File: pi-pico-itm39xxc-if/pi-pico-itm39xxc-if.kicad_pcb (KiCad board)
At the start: 2 copper layers, 113 parts, among them J10 Conn_01x03, J11 Conn_02x04_Odd_Even, J3 Conn_01x03, J4 Conn_01x02, J5 Conn_02x05_Odd_Even, J6 Conn_01x10, J8 Conn_01x02, J9 Conn_01x02, U1 Pico, U10 Opamp_Dual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

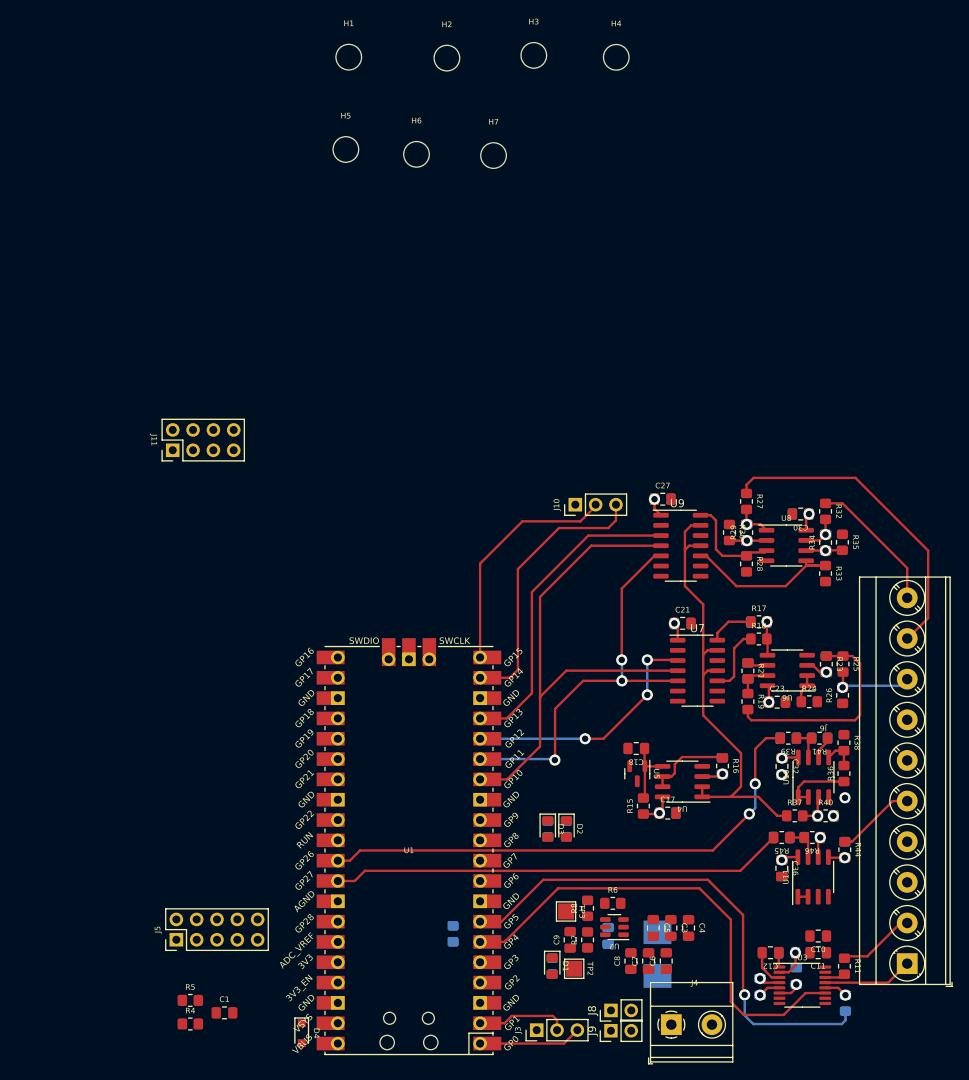
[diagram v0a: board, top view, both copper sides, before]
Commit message: Finishing pi pico itm if pcb
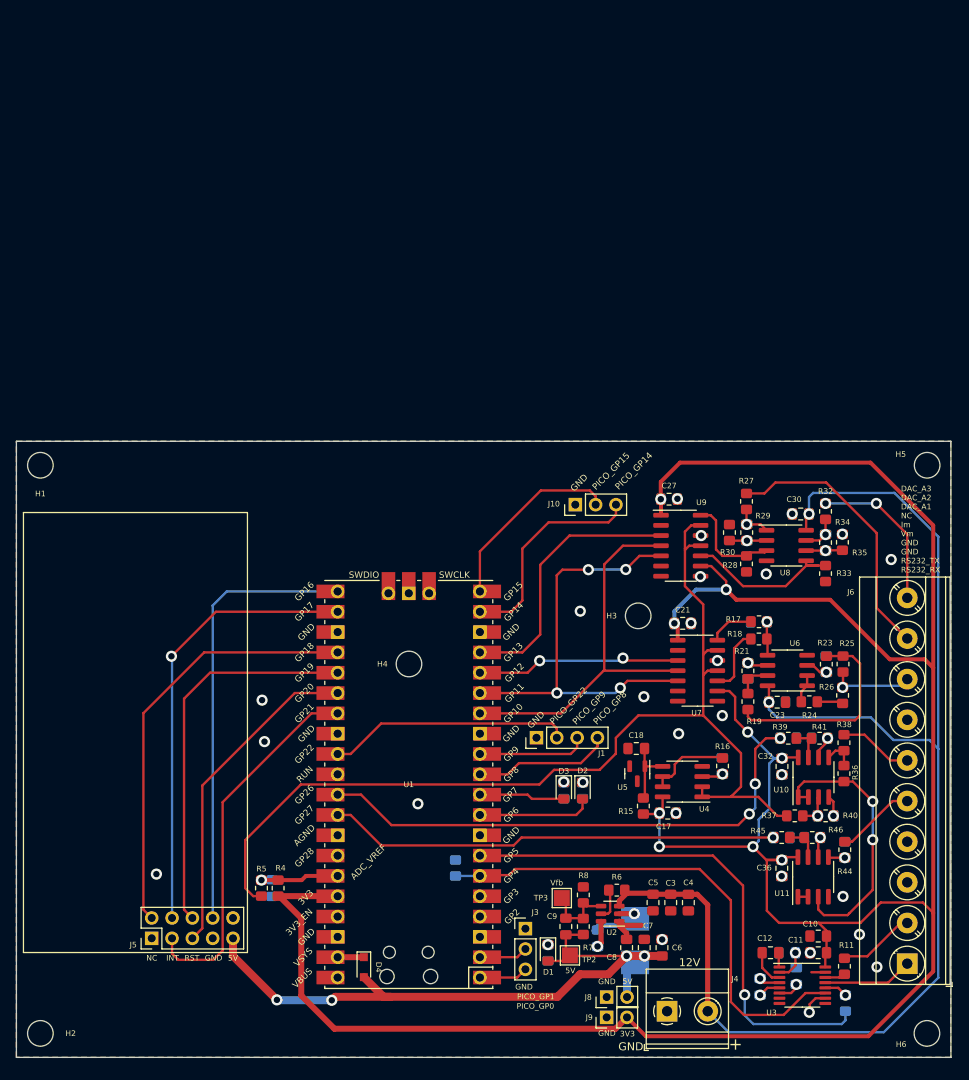
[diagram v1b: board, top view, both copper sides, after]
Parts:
- removed H7: MountingHole, MountingHole:MountingHole_3.2mm_M3
- removed J11: Conn_02x04_Odd_Even, Connector_PinHeader_2.54mm:PinHeader_2x04_P2.54mm_Vertical
- added J1: Conn_01x04, Connector_PinHeader_2.54mm:PinHeader_1x04_P2.54mm_Vertical, F.Cu at (122.2, 69.4)
- C1: moved to B.Cu
- moved H2 132.1 mm to (60.2, 106.4)
- moved H6 127.1 mm to (171.0, 106.4)
- moved H5 82.7 mm to (171.0, 35.4)
- moved H4 80.1 mm to (106.2, 60.2)
- moved H3 71.3 mm to (134.9, 54.2)
- moved H1 63.9 mm to (60.2, 35.4)
- moved R4 20.2 mm to (89.9, 88.2), turned to 90 degrees
- moved C1 16.7 mm to (89.1, 88.2), turned to -90 degrees
- moved R5 16.6 mm to (87.8, 88.2), turned to 90 degrees
- moved J3 12.8 mm to (120.8, 93.3), turned to 0 degrees
- moved D4 11.3 mm to (100.6, 98.1)
- moved U1 8.26 mm to (106.2, 75.3)
- moved R10 8.24 mm to (112.1, 85.7)
- moved D2 5.19 mm to (127.9, 76.1)
- moved R2 5.19 mm to (127.9, 76.1)
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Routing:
- net +3V3: track 13.1 -> 343.6 mm, vias 5 -> 9
- net +12V: track 4.31 -> 163.1 mm
- net +5V: track 0.00 -> 84.6 mm, vias 0 -> 4
- net /DAC_REF: track 57.8 -> 131.1 mm
- net /PICO_GPIO17: track 0.00 -> 55.8 mm, vias 0 -> 1
- net /PICO_GPIO16: track 0.00 -> 55.4 mm
- net /PICO_GPIO18: track 0.00 -> 53.5 mm
- net /PICO_GPIO19: track 0.00 -> 48.4 mm
- net /PICO_GPIO21: track 0.00 -> 46.6 mm
- net /PICO_GPIO20: track 0.00 -> 41.3 mm
- net /PICO_GPIO22: track 0.00 -> 30.4 mm
- net /itm39xxc_meas_cond/V_ref': track 8.49 -> 34.2 mm, vias 0 -> 2
- net /PICO_GPIO8: track 0.00 -> 17.2 mm
- net /DAC_SCLK: track 64.4 -> 48.3 mm
- net /LED_1: track 0.00 -> 14.4 mm
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- added copper zone on B.Cu, net GND
- added copper zone on F.Cu, net GND
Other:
- board outline added: 116.8 x 77 mm
- board text added: "+"
- board text added: "12V"
- board text added: "3V3"
- board text added: "5V"
- board text added: "DAC_A3 DAC_A2 DAC_A1 NC Im Vm GND GND RS232_TX RS232_RX"
- board text added: "GND"
- board text added: "INT"
- board text added: "NC"
- board text added: "PICO_GP0"
- board text added: "PICO_GP1"
- board text added: "PICO_GP14"
- board text added: "PICO_GP15"
- board text added: "PICO_GP22"
- board text added: "PICO_GP8"
- board text added: "PICO_GP9"
- board text added: "RST"
- board text added: "Vfb"
